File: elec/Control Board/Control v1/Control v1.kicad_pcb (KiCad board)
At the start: 2 copper layers, 126.3 x 160 mm, 169 parts, among them J1 DB9_Female_MountingHoles, J10 Conn_02x12_Odd_Even, J12 Screw_Terminal_01x02, J13 Screw_Terminal_01x02, J15 DB25_Female_MountingHoles, J16 Conn_01x04, J17 Conn_01x05, J18 Conn_01x04, J19 Conn_01x07, J2 Conn_01x08, J20 Conn_01x04_Pin, J21 RJ12_6P6C_HORZ, J22 0.100_2Pin, J23 0.100_2Pin, J24 Conn_01x04, J3 Conn_01x08, J4 Conn_01x08, J5 Conn_01x08, J6 Conn_01x08, J7 Conn_02x18_Odd_Even, J8 Conn_01x10, J9 Conn_01x10, Q1 BSS138, Q10 BSS138, Q2 NCE01P30K, Q3 BSS138, Q4 BSS138, Q5 BSS138, Q6 BSS138, Q7 BSS138, Q8 BSS138, Q9 BSS138

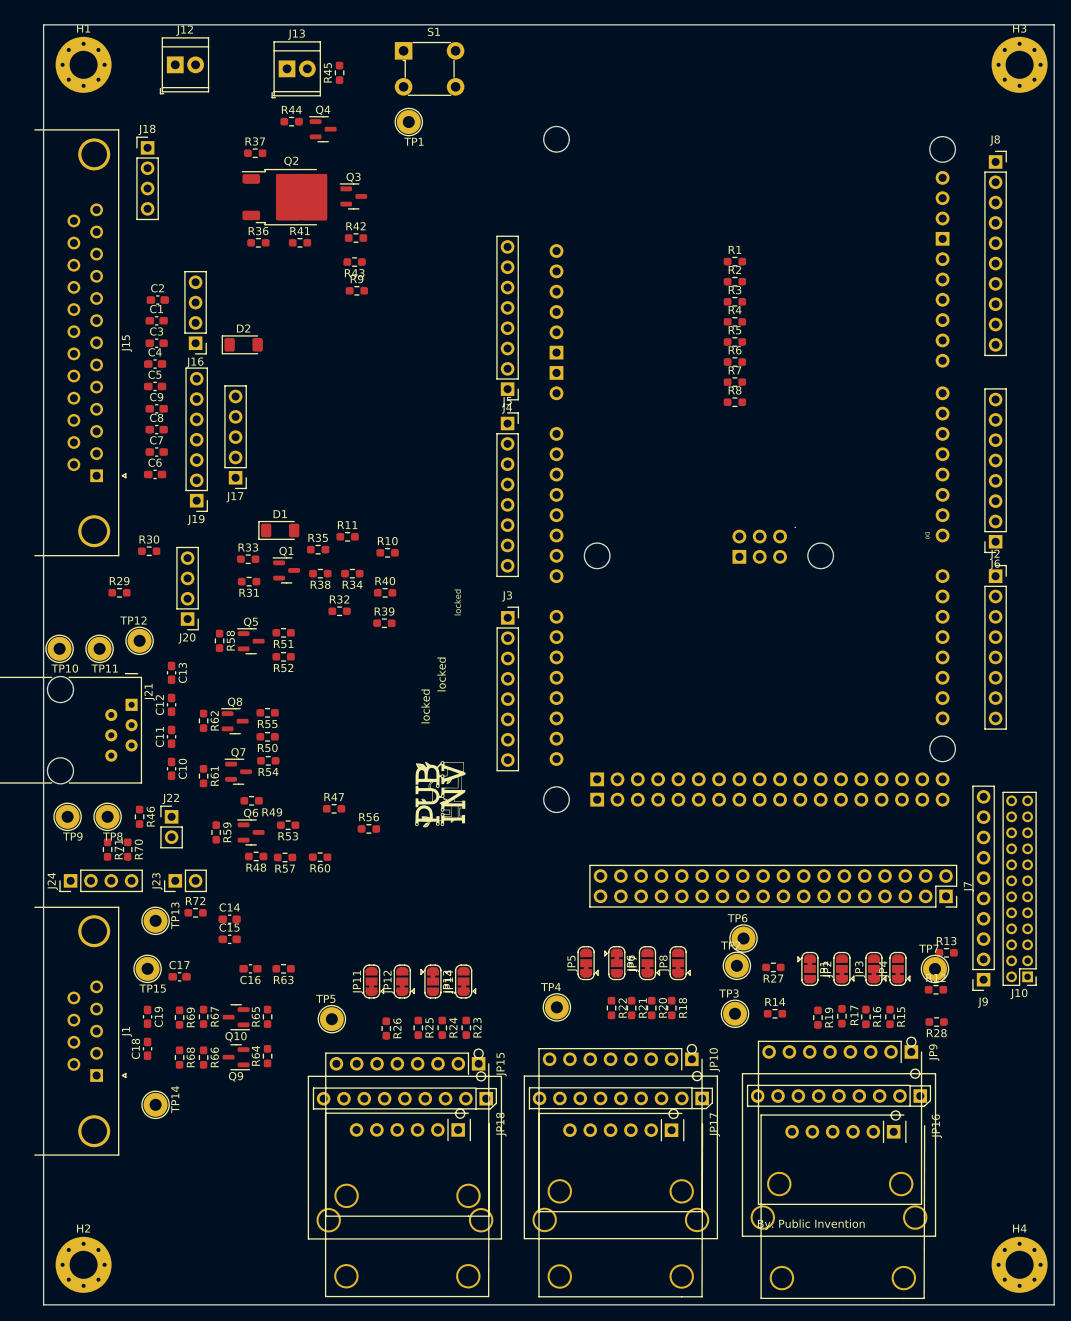
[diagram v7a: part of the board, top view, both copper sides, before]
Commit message: Place PCB components.
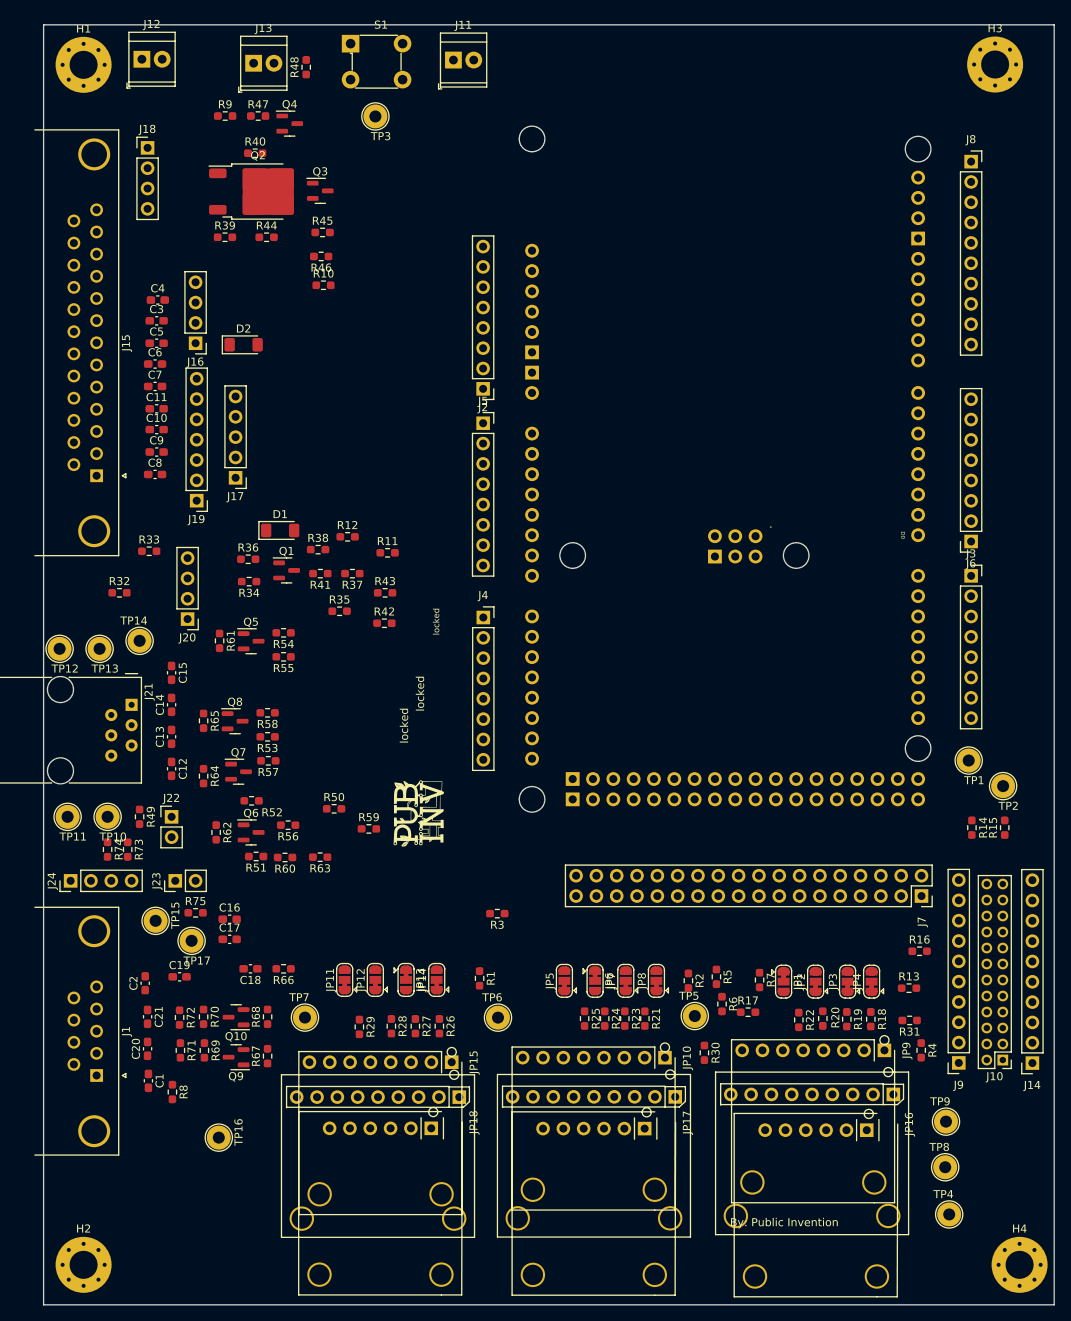
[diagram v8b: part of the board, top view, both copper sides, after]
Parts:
- added C1: 39PF, Capacitor_SMD:C_0603_1608Metric_Pad1.08x0.95mm_HandSolder, F.Cu at (63.1, 182.0)
- added C2: 39PF, Capacitor_SMD:C_0603_1608Metric_Pad1.08x0.95mm_HandSolder, F.Cu at (62.7, 169.8)
- added J11: Screw_Terminal_01x02, TerminalBlock_TE-Connectivity:TerminalBlock_TE_282834-2_1x02_P2.54mm_Horizontal, F.Cu at (101.2, 54.4)
- added J14: Conn_01x08, Connector_PinSocket_2.54mm:PinSocket_1x10_P2.54mm_Vertical, F.Cu at (173.6, 179.8)
- added R14: 1R0, Resistor_SMD:R_0603_1608Metric_Pad0.98x0.95mm_HandSolder, F.Cu at (166.0, 150.4)
- added R15: 1R0, Resistor_SMD:R_0603_1608Metric_Pad0.98x0.95mm_HandSolder, F.Cu at (170.1, 150.4)
- added R8: 1R0, Resistor_SMD:R_0603_1608Metric_Pad0.98x0.95mm_HandSolder, F.Cu at (66.1, 183.4)
- added TP1: TX, TestPoint:TestPoint_Loop_D2.54mm_Drill1.5mm_Beaded, F.Cu at (165.6, 142.0)
- added TP2: RX, TestPoint:TestPoint_Loop_D2.54mm_Drill1.5mm_Beaded, F.Cu at (169.9, 145.2)
- moved R1 95.1 mm to (104.5, 169.2), turned to -90 degrees
- moved R4 94.0 mm to (159.7, 178.2), turned to -90 degrees
- moved R2 87.6 mm to (130.6, 169.5), turned to -90 degrees
- moved R3 82.0 mm to (106.7, 161.1), turned to 180 degrees
- moved R6 80.3 mm to (134.8, 172.4), turned to -90 degrees
- moved R5 79.4 mm to (134.1, 169.0), turned to -90 degrees
- moved R7 74.8 mm to (139.5, 169.4), turned to -90 degrees
- moved R9 73.1 mm to (72.7, 61.4)
- moved TP4 40.9 mm to (163.2, 198.7)
- moved TP8 38.1 mm to (162.7, 192.8)
- moved TP9 19.1 mm to (162.8, 187.1)
- moved R30 13.7 mm to (132.6, 178.5), turned to -90 degrees
- moved J10 10.9 mm to (169.9, 179.4)
- moved J9 10.9 mm to (164.4, 179.8)
- moved TP16 8.90 mm to (71.9, 189.1)
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- renumbered C8 to C10, C9 to C11, C10 to C12, C11 to C13, C12 to C14, C13 to C15, C14 to C16, C15 to C17, C16 to C18, C17 to C19, C18 to C20, C19 to C21, C1 to C3, C2 to C4, C3 to C5, C4 to C6, C5 to C7, C6 to C8, C7 to C9, J4 to J2, J2 to J3, J3 to J4, R9 to R10, R10 to R11, R11 to R12, R12 to R13, R13 to R16, R14 to R17, R15 to R18, R16 to R19, R17 to R20, R18 to R21, R19 to R22, R20 to R23, R21 to R24, R22 to R25, R23 to R26, R24 to R27, R25 to R28, R26 to R29, R27 to R30, R28 to R31, R29 to R32, R30 to R33, R31 to R34, R32 to R35, R33 to R36, R34 to R37, R35 to R38, R36 to R39, R37 to R40, R38 to R41, R39 to R42, R40 to R43, R41 to R44, R42 to R45, R43 to R46, R44 to R47, R45 to R48, R46 to R49, R47 to R50, R48 to R51, R49 to R52, R50 to R53, R51 to R54, R52 to R55, R53 to R56, R54 to R57, R55 to R58, R56 to R59, R57 to R60, R58 to R61, R59 to R62, R60 to R63, R61 to R64, R62 to R65, R63 to R66, R64 to R67, R65 to R68, R66 to R69, R67 to R70, R68 to R71, R69 to R72, R70 to R73, R71 to R74, R72 to R75, R8 to R9, TP8 to TP10, TP9 to TP11, TP10 to TP12, TP11 to TP13, TP12 to TP14, TP13 to TP15, TP14 to TP16, TP15 to TP17, TP1 to TP3, TP2 to TP4, TP3 to TP5, TP4 to TP6, TP5 to TP7, TP6 to TP8, TP7 to TP9
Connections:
- A1 pad 5V3: 5V3 -> +5V
- A1 pad 5V4: 5V4 -> +5V
- A1 pad D34: Net-(J7-Pin_15) -> D34
- A1 pad VIN: Net-(J4-Pin_1) (its old number) -> +12V
- J1 pad 1: unconnected-(J1-Pad1) -> D35
- J1 pad 5: unconnected-(J1-Pad5) -> Net-(C2-Pad1)
- J10 pad 23: /D_PSU_RX -> /TX
- J10 pad 24: /D_PSU_TX -> /RX
- J13 pad 1: /SSR Interface/+24V_SSR -> +24V
- J2 pad 1: Net-(J4-Pin_1) (its old number) -> +12V
- J7 pad 15: Net-(J7-Pin_15) -> D34
- R1 pad 1: unconnected-(R1-Pad1) -> D35
- R3 pad 1: unconnected-(R3-Pad1) -> D34
- R7 pad 1: unconnected-(R7-Pad1) -> D33
- R9 pad 1: unconnected-(R8-Pad1) -> D51
